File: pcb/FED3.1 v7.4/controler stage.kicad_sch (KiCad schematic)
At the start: 25 parts, among them IC4 RTC PCF8523T, J1 Conn_02x03_Odd_Even, SW2 SPST_TACT-KMR2, U1 ATSAMD21G18A, U4 Adafruit LCD Screen, X1 ClockXtal, X2 uXtal, X4 microsd

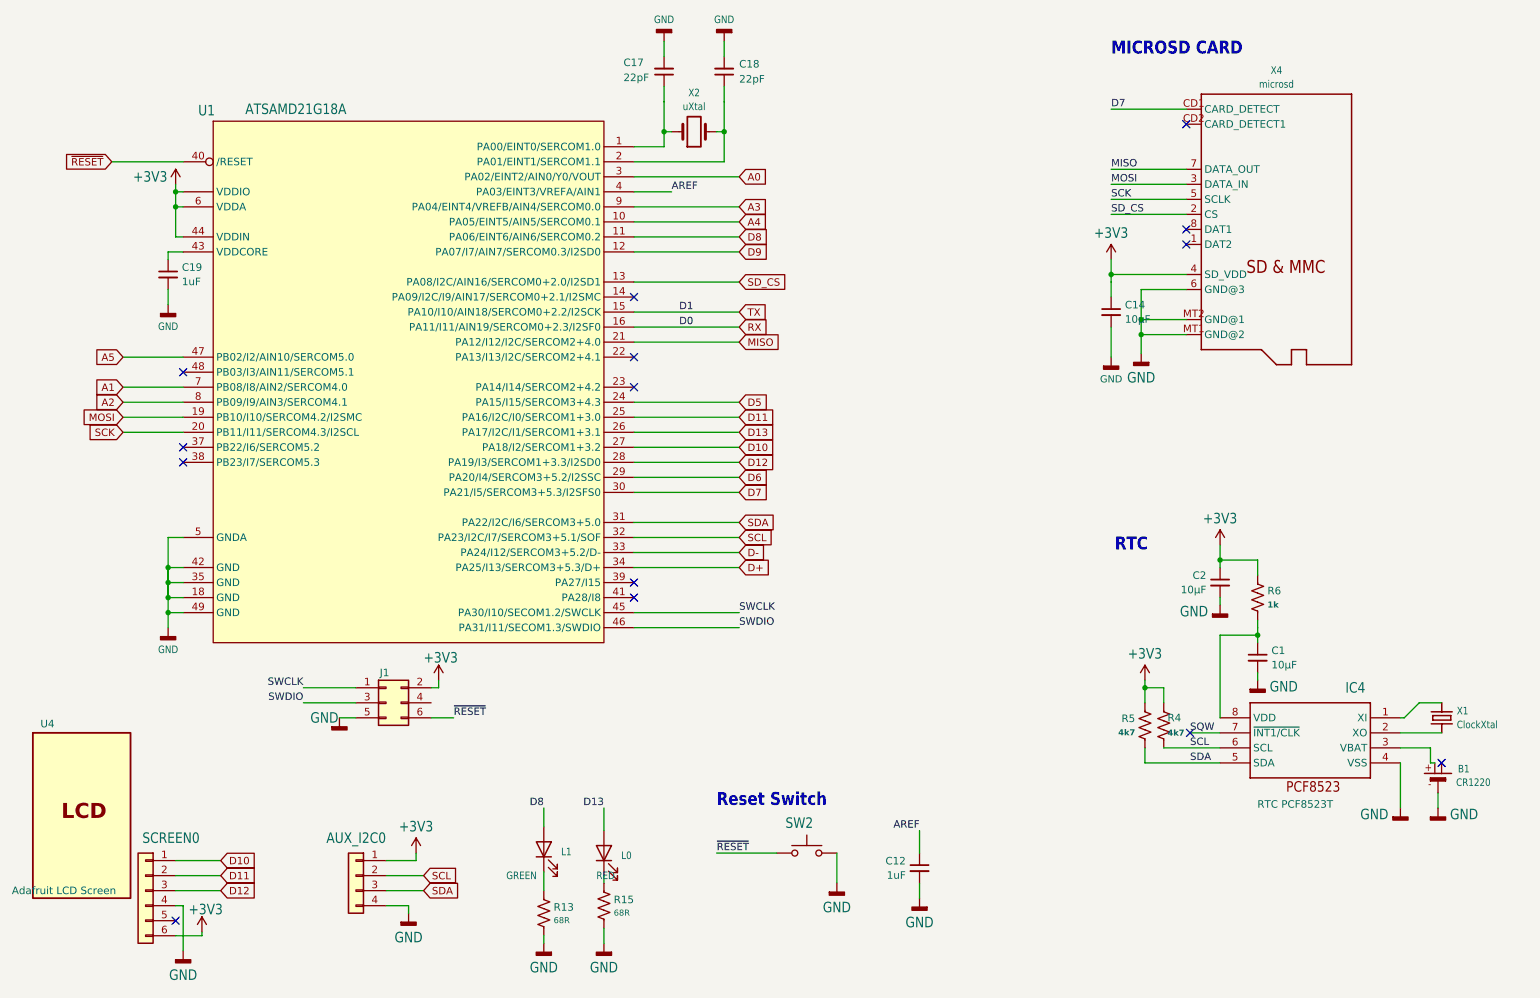
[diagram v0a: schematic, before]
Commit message: review step 2
Realocação de labels e refªs:
- sem qq alteração no circuito
- alteração na PCB apenas a ver com alocação de Designators/SilkScreen parts
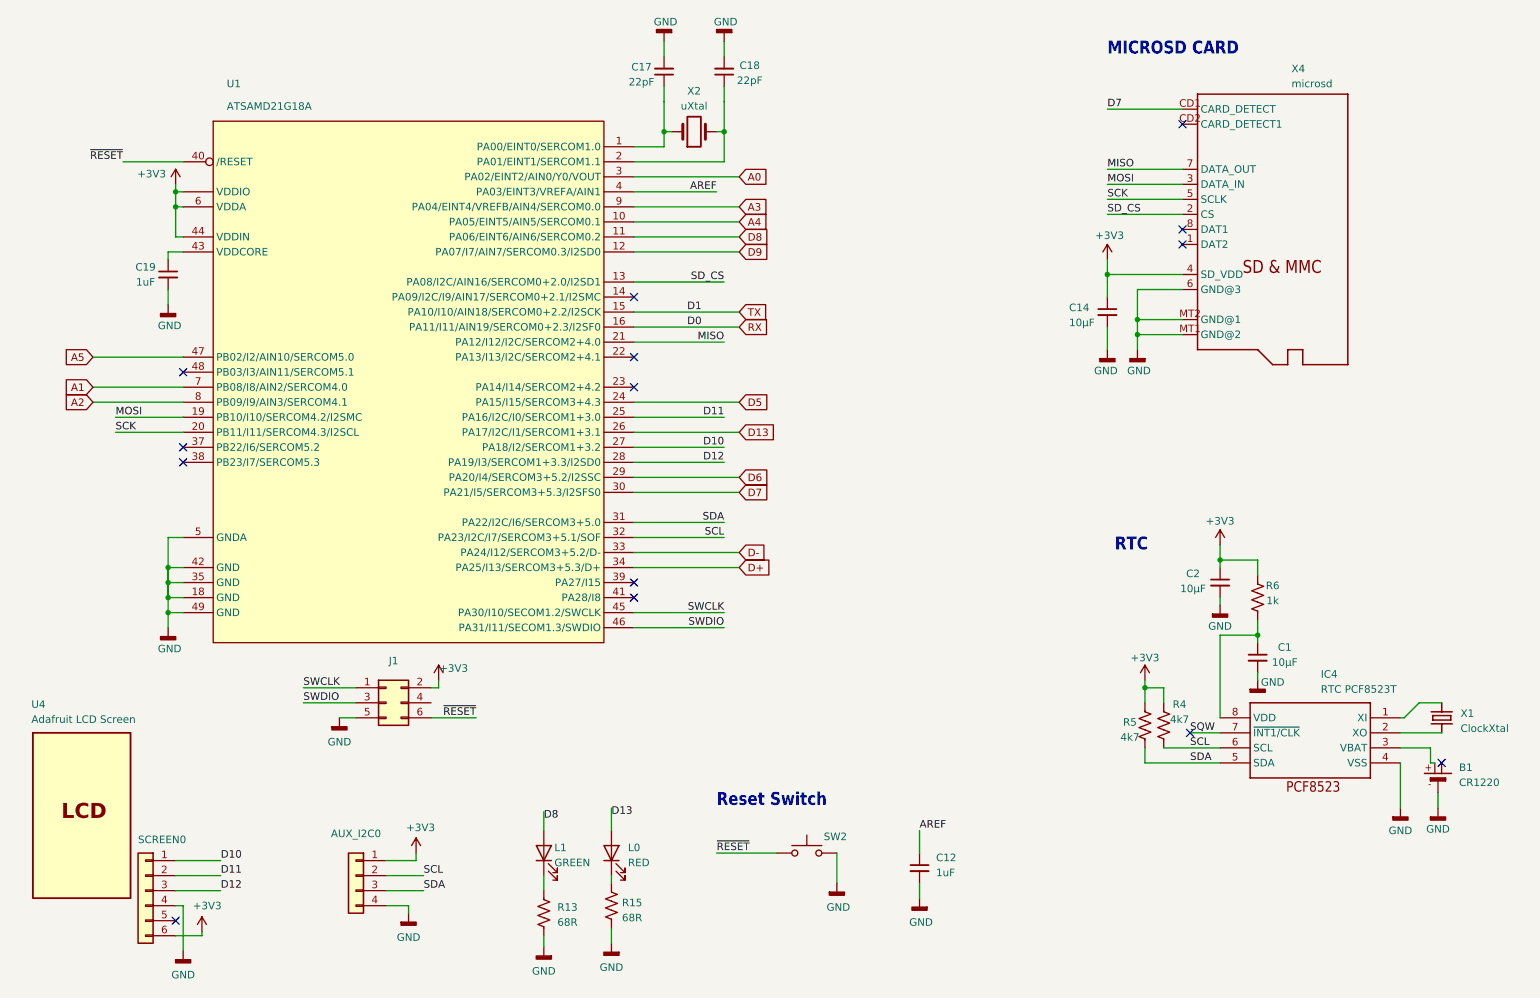
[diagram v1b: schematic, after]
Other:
- moved on the sheet: C14, L0, L1, R15, X4
